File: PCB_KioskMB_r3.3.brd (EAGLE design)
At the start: 172.1 x 103.3 mm, 330 parts, among them IC1 ISL60002DIH325Z-TK, IC18 FT232RL, IC19 MCP6022-I/ST, IC2 SN65HVD12D, IC21 LTC1771EMS8, IC3 PIC24FJ256GA110-I/PT, IC4 PIC10F200T-I/OT, IC5 LM75ADP, IC6 24LC32A-I/MS, IC7 PCF2123TS/1-T, IC8 M25P16-VMN6P, IC9 LM3405AXMK/NOPB, J1 DF11-10DP-2DSA(01), J10 CCM03-3504LFT-NR, J14 3-641215-2, J15 1990834, J16 1990737, J17 14011213102000, J18 14011213102000, J19 14011213102000, J30 22-11-2072, J4 3-641215-2, J45 3-641215-4, J47 DF11-10DP-2DSA(01), J48 3-641215-2, J49 3-641215-2, J50 0039301040, J7 SS-6566-NF, J8 TSW-108-07-G-D, J9 SS-6566-NF, Q14 MAX9938HEUK, Q15 SI4564DY, Q16 CSD87331Q3D, Q18 SI4564DY, Q19 CSD87331Q3D, Q2 FDC6330L, Q20 IPD30N06S2L-23, Q21 IPD30N06S2L-23, Q23 FDN352AP, Q24 BSS138, Q3 SR3.3.TCT, Q4 7B-28.63636MAAJ-T, Q5 FDC6330L, Q6 CM519 32.768KDZF-UT, Q7 SSM6P49NU,LFPZ, U1 LTC1955, U2 LE33, U3 ADS1015, U6 TPS43061, U7 TPS43061, U8 TPA3111D1PWP, U9 OPA322SAIDBVT, X1 FH12-10S-0.5S1.00MM, X2 MINI-USB_4P-85-32004-10X

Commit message: :+1:
:P
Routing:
- net +3.3V/1: track 247.3 -> 245.9 mm
- net ISENSEB: track 83.6 -> 82.2 mm
- net SCL1: track 215.1 -> 213.9 mm
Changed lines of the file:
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@@
 <wire x1="62.12154375" y1="28.2194" x2="61.38494375" y2="28.956" width="0.1524" layer="1"/>
 <wire x1="82.2945125" y1="25.9334" x2="84.57035625" y2="25.9334" width="0.1524" layer="1"/>
-<wire x1="87.82535625" y1="22.6784" x2="88.9762" y2="22.6784" width="0.1524" layer="1"/>
-<wire x1="88.9762" y1="22.6784" x2="90.7466" y2="24.4488" width="0.1524" layer="1"/>
-<wire x1="90.7466" y1="24.4488" x2="90.7466" y2="24.638" width="0.1524" layer="1"/>
+<wire x1="86.47535625" y1="24.0284" x2="84.57035625" y2="25.9334" width="0.1524" layer="1"/>
+<wire x1="86.47535625" y1="24.0284" x2="87.26275625" y2="23.241" width="0" layer="19" extent="1-16"/>
 <wire x1="78.4553125" y1="22.0942" x2="82.2945125" y2="25.9334" width="0.1524" layer="1"/>
-<wire x1="84.57035625" y1="25.9334" x2="87.82535625" y2="22.6784" width="0.1524" layer="1"/>
+<wire x1="90.4696" y1="24.32494375" x2="90.17305625" y2="24.0284" width="0.1524" layer="1"/>
+<wire x1="90.17305625" y1="24.0284" x2="86.47535625" y2="24.0284" width="0.1524" layer="1"/>
+<wire x1="90.7466" y1="24.638" x2="90.4696" y2="24.361" width="0.1524" layer="1"/>
+<wire x1="90.4696" y1="24.361" x2="90.4696" y2="24.32494375" width="0.1524" layer="1"/>
 <wire x1="27.5082" y1="43.1038" x2="16.51" y2="51.435" width="0" layer="19" extent="1-1"/>
 </signal>
@@
 <wire x1="13.462" y1="52.705" x2="16.256" y2="49.911" width="0.1524" layer="16"/>
 <wire x1="16.256" y1="49.911" x2="16.891" y2="49.911" width="0.1524" layer="16"/>
-<wire x1="87.9516125" y1="22.9832" x2="88.6968" y2="22.9832" width="0.1524" layer="1"/>
-<wire x1="88.6968" y1="22.9832" x2="90.1648" y2="24.4512" width="0.1524" layer="1"/>
-<wire x1="90.1648" y1="24.4512" x2="90.1648" y2="24.87899375" width="0.1524" layer="1"/>
+<wire x1="84.6966125" y1="26.2382" x2="86.6016125" y2="24.3332" width="0.1524" layer="1"/>
+<wire x1="86.6016125" y1="24.3332" x2="89.61900625" y2="24.3332" width="0.1524" layer="1"/>
+<wire x1="89.61900625" y1="24.3332" x2="90.1648" y2="24.87899375" width="0.1524" layer="1"/>
 <wire x1="90.1648" y1="24.87899375" x2="91.57480625" y2="26.289" width="0.1524" layer="1"/>
 <wire x1="78.32905625" y1="22.399" x2="82.16825625" y2="26.2382" width="0.1524" layer="1"/>
 <wire x1="82.16825625" y1="26.2382" x2="84.6966125" y2="26.2382" width="0.1524" layer="1"/>
-<wire x1="84.6966125" y1="26.2382" x2="87.9516125" y2="22.9832" width="0.1524" layer="1"/>
 <wire x1="91.57480625" y1="26.289" x2="94.5058" y2="26.289" width="0.1524" layer="1"/>
 <wire x1="15.6464" y1="51.689" x2="21.336" y2="65.278" width="0" layer="19" extent="1-1"/>
@@
 <wire x1="95.92279375" y1="28.2932" x2="95.44080625" y2="28.2932" width="0.1524" layer="16"/>
 <wire x1="82.042" y1="26.543" x2="84.82286875" y2="26.543" width="0.1524" layer="1"/>
-<wire x1="88.07786875" y1="23.288" x2="88.519" y2="23.288" width="0.1524" layer="1"/>
-<wire x1="88.519" y1="23.288" x2="89.86" y2="24.629" width="0.1524" layer="1"/>
-<wire x1="89.86" y1="24.629" x2="89.86" y2="25.00525" width="0.1524" layer="1"/>
+<wire x1="84.82286875" y1="26.543" x2="86.70246875" y2="24.6634" width="0.1524" layer="1"/>
+<wire x1="86.70246875" y1="24.6634" x2="89.51815" y2="24.6634" width="0.1524" layer="1"/>
+<wire x1="89.51815" y1="24.6634" x2="92.3214" y2="27.46665" width="0.1524" layer="1"/>
 <wire x1="92.3214" y1="27.46665" x2="92.3214" y2="27.813" width="0.1524" layer="1"/>
 <wire x1="78.232" y1="22.733" x2="82.042" y2="26.543" width="0.1524" layer="1"/>
-<wire x1="84.82286875" y1="26.543" x2="88.07786875" y2="23.288" width="0.1524" layer="1"/>
-<wire x1="89.86" y1="25.00525" x2="92.3214" y2="27.46665" width="0.1524" layer="1"/>
 </signal>
 <signal name="N$6">

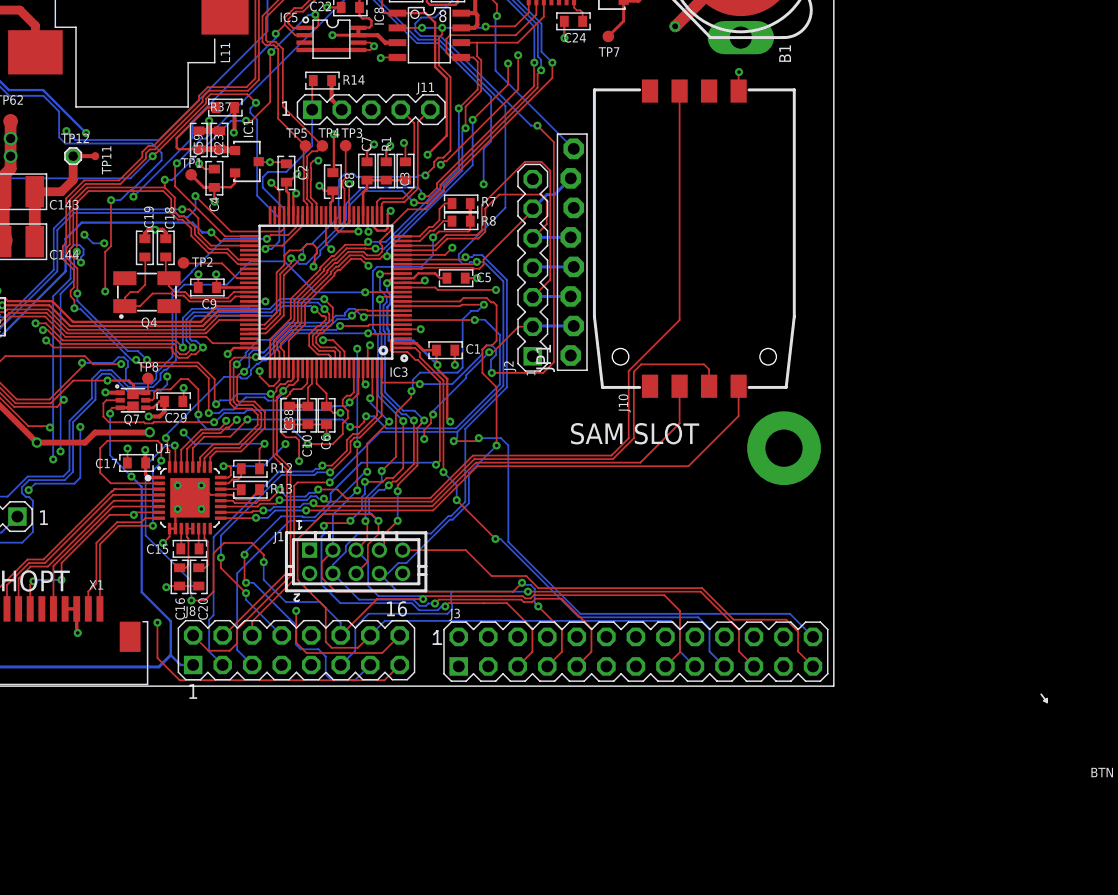
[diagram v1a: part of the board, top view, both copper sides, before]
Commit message: added .png of connectors.
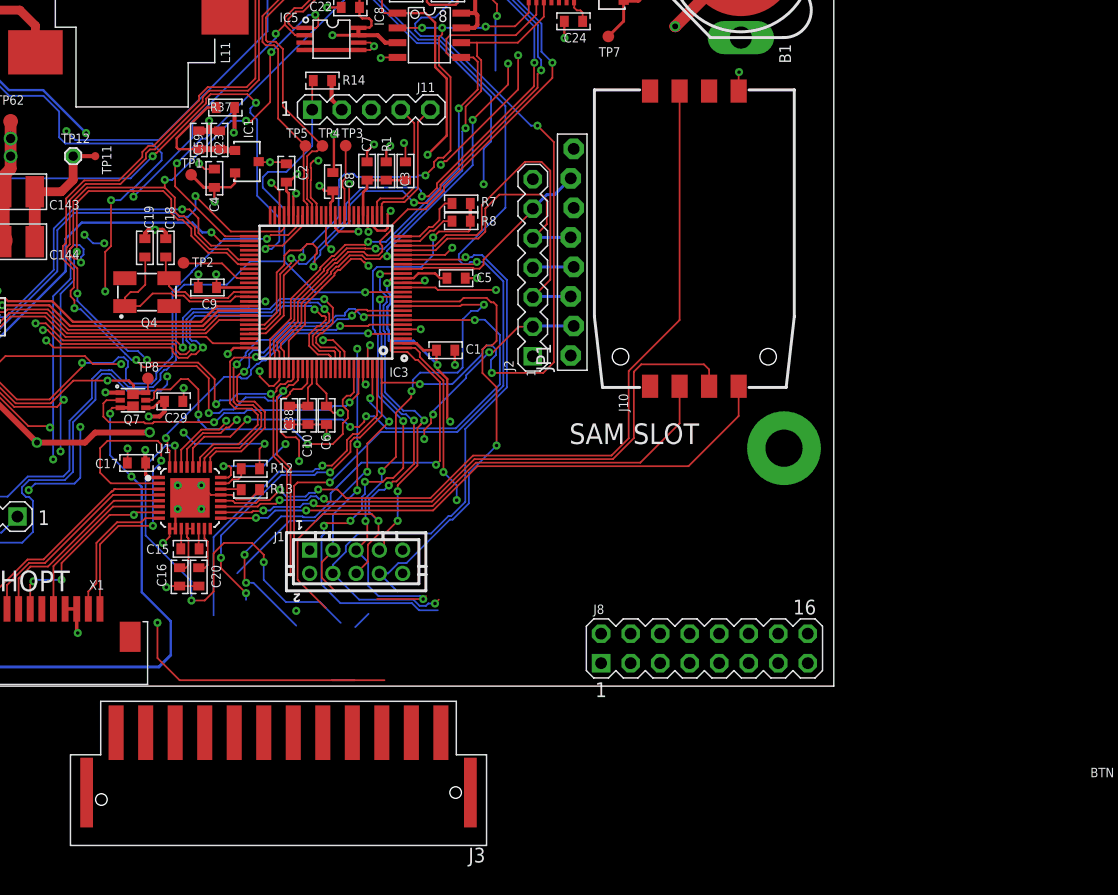
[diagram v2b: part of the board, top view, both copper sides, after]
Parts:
- J3: value (none) -> 14011213102000; device CON-pinHeader-AON:MA13-2 -> elock_lib:14011213102000
- moved J8 35.1 mm to (145.9, 3.24)
- moved J3 32.8 mm to (109.2, -8.41), turned to 180 degrees
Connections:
- net +3.3V: no longer J3.25
- net +3.3V/2: no longer J8.1
- net +SMB: no longer J3.13, J8.7
- net /CL_CS1: no longer J3.19
- net CL_IRQ: no longer J3.9
- net CM_RST: no longer J8.5
- net DGND: no longer J3.23
- net PHOTOCELL: no longer J3.5
- net PIC_INT: no longer J3.7
- net SCLK2: no longer J3.15
- net SDA1: no longer JP1.8
- net SDI2: no longer J3.21
- net SDO2: no longer J3.17
- net U2CTL: no longer J3.26, J8.6
- net U2RX: no longer J8.4
- net U2TX: no longer J8.2
- net VPS_ON: no longer J8.8
- net VPS_SEN: no longer J8.3
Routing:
- net U2CTL: track 163.9 -> 113.7 mm, vias 5 -> 3
- net SDI2: track 88.9 -> 41.8 mm, vias 2 -> 1
- net +3.3V: track 418.4 -> 376.3 mm
- net SDO2: track 83.9 -> 45.4 mm
- net SCLK2: track 120.8 -> 87.4 mm
- net DGND: track 474.3 -> 443.3 mm
- net /CL_CS1: track 45.8 -> 15.7 mm, vias 3 -> 2
- net +SMB: track 338.0 -> 309.9 mm
- net PIC_INT: track 61.7 -> 35.9 mm, vias 6 -> 4
- net CL_IRQ: track 73.9 -> 55.8 mm
- net PHOTOCELL: track 70.3 -> 57.2 mm, vias 6 -> 5
- net SCL1: track 213.9 -> 201.3 mm
- net U2TX: track 120.3 -> 108.0 mm
- net SDA1: track 239.0 -> 227.7 mm
- net /RAM_CS: track 54.0 -> 45.3 mm
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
